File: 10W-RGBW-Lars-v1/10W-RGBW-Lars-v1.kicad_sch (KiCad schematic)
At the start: 60 parts, among them J1 USB_C_Receptacle_USB2.0_16P, J101 Conn_Coaxial, SW1 SW_SPST, SW2 SW_SPST, U1 CH224D, U101 ESP32-C6FHx, Y1 40MHz

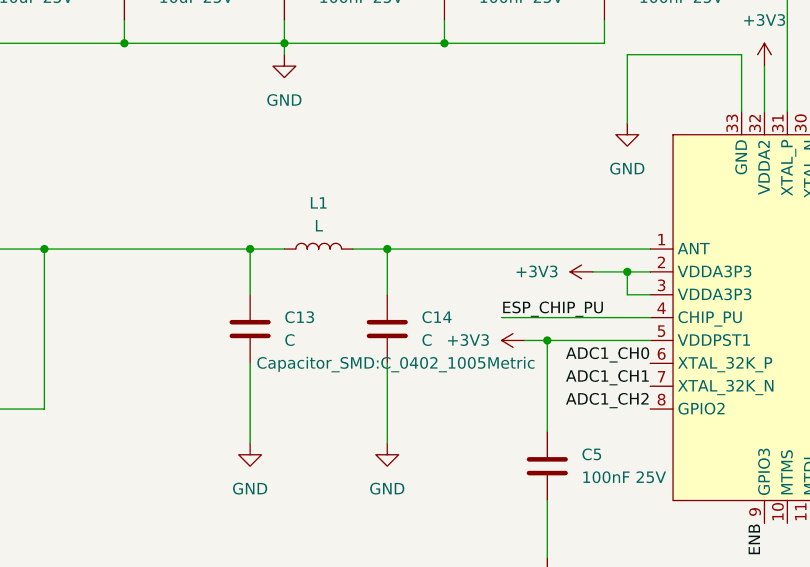
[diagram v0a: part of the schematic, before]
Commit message: added fiducials, fixed shunt resistor size
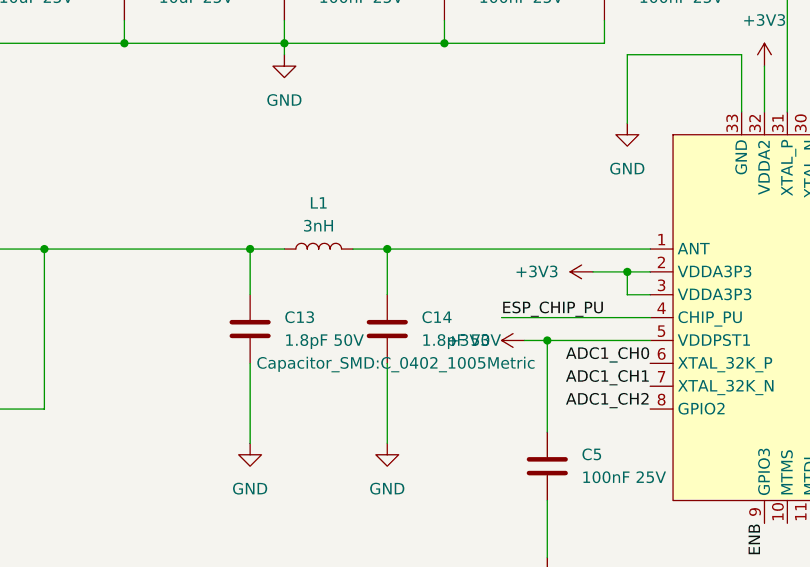
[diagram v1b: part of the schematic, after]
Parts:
- C13, C14: value C -> 1.8pF 50V
- L1: value L -> 3nH
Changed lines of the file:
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@@
 			)
 		)
-		(property "Value" "C"
+		(property "Value" "1.8pF 50V"
 			(at 144.78 109.2199 0)
 			(effects
@@
 			)
 		)
-		(property "Value" "C"
+		(property "Value" "1.8pF 50V"
 			(at 129.54 109.2199 0)
 			(effects
@@
 			)
 		)
-		(property "Value" "L"
+		(property "Value" "3nH"
 			(at 133.35 96.52 90)
 			(effects
@@
 		)
 		(instances
-			(project "HelixQueledPrint"
+			(project "10W-RGBW-Lars-v1"
 				(path "/398fd733-417c-46a8-b62a-83839861ebca"
 					(page "2")
@@
 		)
 		(instances
-			(project "HelixQueledPrint"
+			(project "10W-RGBW-Lars-v1"
 				(path "/398fd733-417c-46a8-b62a-83839861ebca"
 					(page "4")
@@
 		)
 		(instances
-			(project "HelixQueledPrint"
+			(project "10W-RGBW-Lars-v1"
 				(path "/398fd733-417c-46a8-b62a-83839861ebca"
 					(page "5")
@@
 		)
 		(instances
-			(project "HelixQueledPrint"
+			(project "10W-RGBW-Lars-v1"
 				(path "/398fd733-417c-46a8-b62a-83839861ebca"
 					(page "6")
@@
 		)
 		(instances
-			(project "HelixQueledPrint"
+			(project "10W-RGBW-Lars-v1"
 				(path "/398fd733-417c-46a8-b62a-83839861ebca"
 					(page "3")
